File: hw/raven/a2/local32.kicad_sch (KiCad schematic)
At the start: 94 parts, among them J301 SIMM72, J302 SIMM72, J303 SIMM72, J304 SIMM72, J305 PWM, J306 Pinhdr_01x03, J307 USB2Header, J308 ARGB, U301 CH559L, U302 CH334R, U303 XR68M752, U304 CH213K, U305 MAX3245CAI+T, U306 W5100S-L, U307 74LVC1G19, X301 24Mhz (3.3V), Y301 12Mhz, Y302 25Mhz

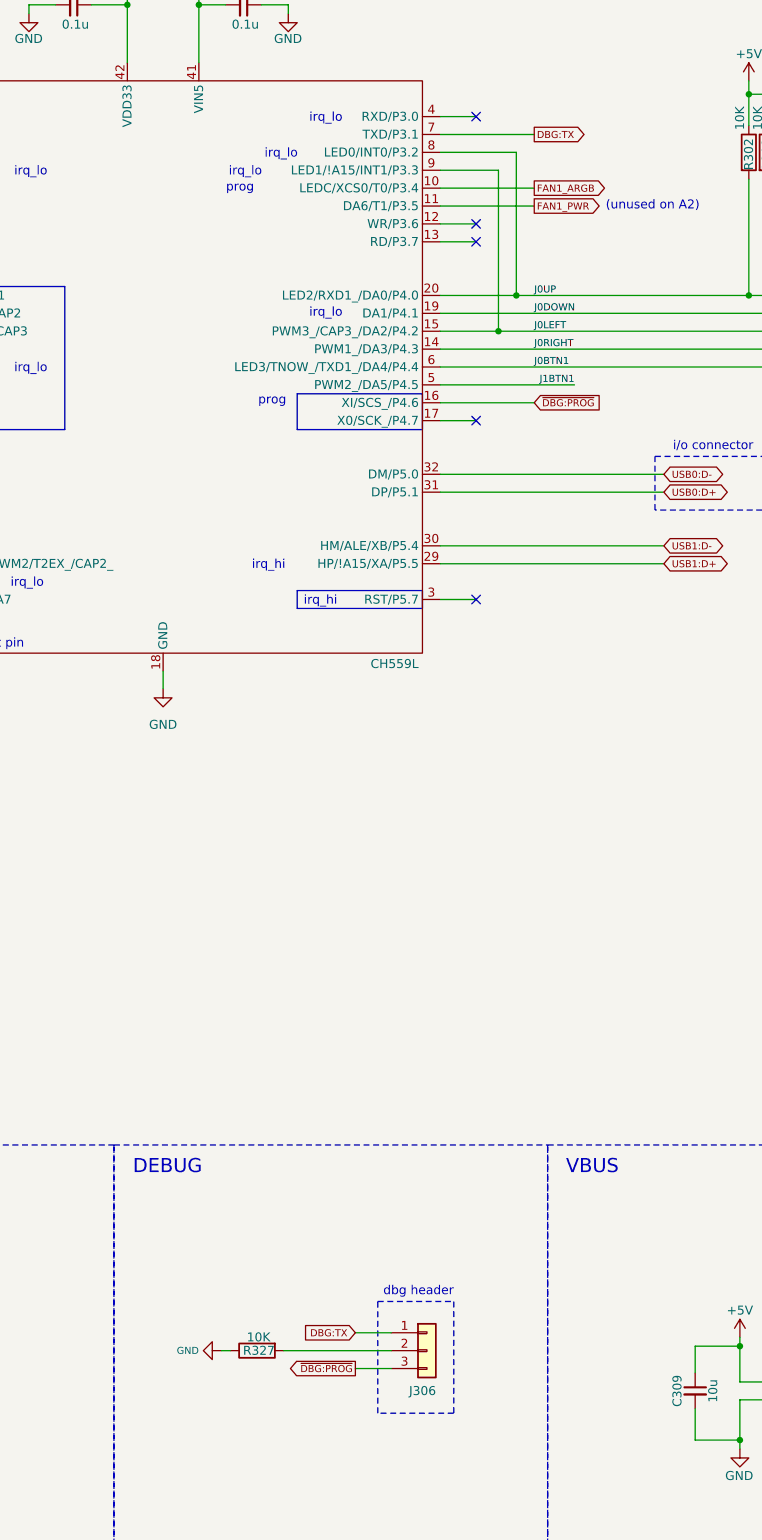
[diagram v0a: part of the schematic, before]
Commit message: minor fixes
- replace IDE header footprint and part
- fix floating (unused) inputs on U102
- removed ckbd debug pads
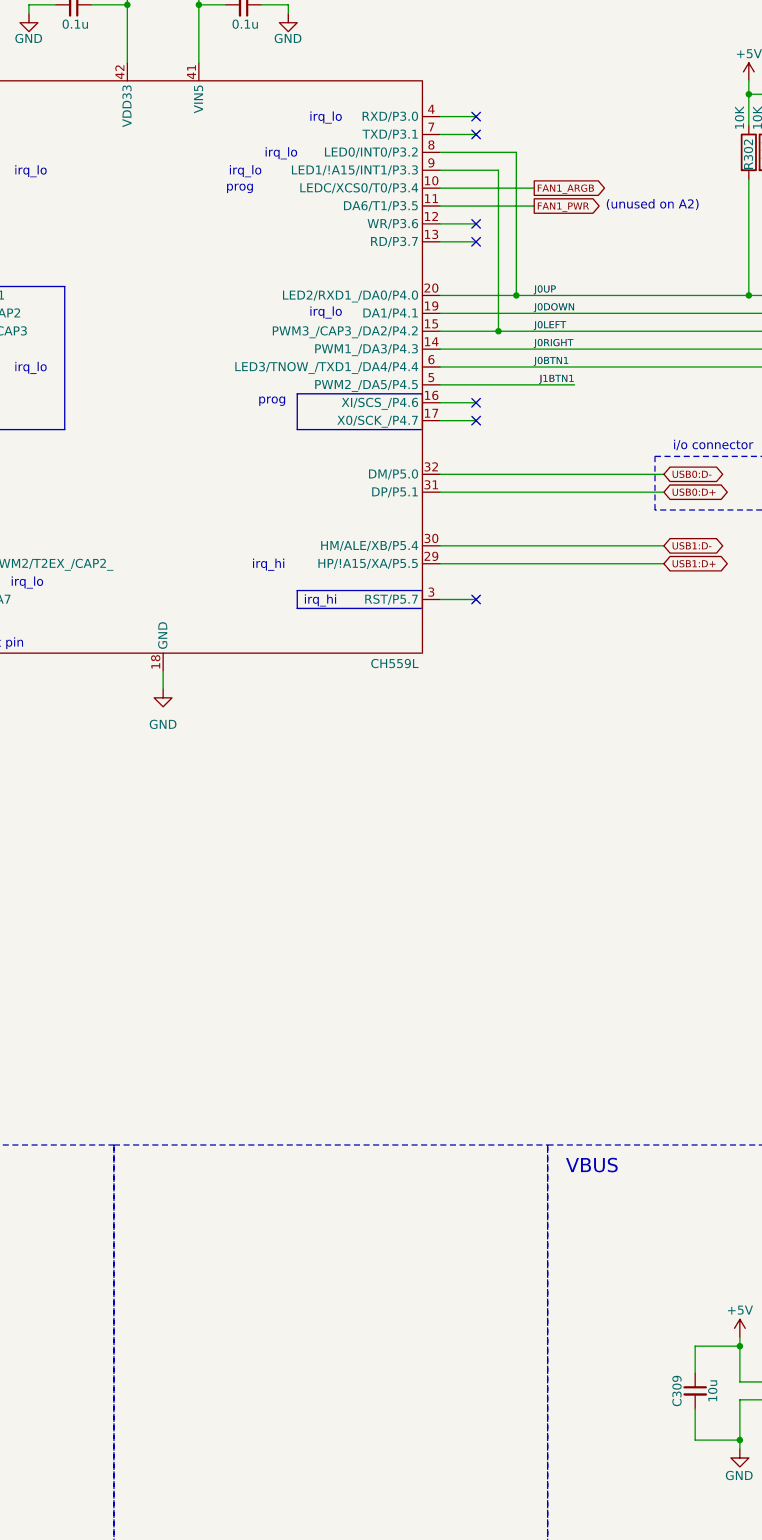
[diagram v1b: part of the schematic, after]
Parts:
- removed J306: Pinhdr_01x03, Connector_PinHeader_2.54mm:PinHeader_1x03_P2.54mm_Vertical, symbol Connector_Generic:Conn_01x03
- removed R327: 10K, Resistor_SMD:R_1206_3216Metric_Pad1.30x1.75mm_HandSolder, symbol Device:R
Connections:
- net DBG:TX: no longer names the net of U301.7 (TXD/P3.1)
- net ~{DBG:PROG}: no longer names the net of U301.16 (XI/SCS_/P4.6)
- no-connect marks 34 -> 36
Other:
- note removed: "DEBUG"
- note removed: "dbg header"

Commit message: A2 rework
- reworking top-left area for dsp56303
- internal speaker header for YM
- software controlled volume for YM
- misc routing cleanup
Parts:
- removed C303, C304, C328, C329: 33p, Capacitor_SMD:C_1206_3216Metric_Pad1.33x1.80mm_HandSolder, symbol 68k:c_100nf_smd1206
- removed C306, C307: 10u, Capacitor_SMD:C_1206_3216Metric_Pad1.33x1.80mm_HandSolder, symbol 68k:c_100nf_smd1206
- removed C316, C317, C318, C319, C320, C321, C322, C323, C324, C325, C326, C327: 0.1u, Capacitor_SMD:C_1206_3216Metric_Pad1.33x1.80mm_HandSolder, symbol 68k:c_100nf_smd1206
- removed J307: USB2Header, 68k:USB2Header, symbol 68k:USB2Header
- removed L301, L302, L303: 120, Inductor_SMD:L_1206_3216Metric_Pad1.42x1.75mm_HandSolder, symbol Device:L_Small
- removed R301, R317, R324: 1K, Resistor_SMD:R_1206_3216Metric_Pad1.30x1.75mm_HandSolder, symbol Device:R
- removed R332, R334: 49.9, Resistor_SMD:R_1206_3216Metric_Pad1.30x1.75mm_HandSolder, symbol Device:R
- removed R340, R341: 10K, Resistor_SMD:R_1206_3216Metric_Pad1.30x1.75mm_HandSolder, symbol Device:R
- removed R342: 1M, Resistor_SMD:R_1206_3216Metric_Pad1.30x1.75mm_HandSolder, symbol Device:R
- removed R343: 12.3K, Resistor_SMD:R_1206_3216Metric_Pad1.30x1.75mm_HandSolder, symbol Device:R
- removed U302: CH334R, Package_SO:QSOP-16_3.9x4.9mm_P0.635mm, symbol 68k:CH334R
- removed U306: W5100S-L, Package_QFP:LQFP-48_7x7mm_P0.5mm, symbol 68k:W5100S-L
- removed U307: 74LVC1G19, Package_TO_SOT_SMD:SOT-23-6_Handsoldering, symbol 74xGxx:74LVC1G19
- removed Y301: 12Mhz, 68k:ECS120203XENTR, symbol Device:Crystal
- removed Y302: 25Mhz, 68k:ECS120203XENTR, symbol Device:Crystal
- added J306: ESSI0, 68k:ESSI, symbol 68k:ESSI
- added J307: ESSI1, 68k:ESSI, symbol 68k:ESSI
- added R125, R126, R127, R128, R129, R130, R131: 1K, Resistor_SMD:R_1206_3216Metric_Pad1.30x1.75mm_HandSolder, symbol Device:R
- added R132, R133, R134, R135, R137, R138, R139, R140, R141, R143: 33, Resistor_SMD:R_1206_3216Metric_Pad1.30x1.75mm_HandSolder, symbol Device:R
- added R327: 10K, Resistor_SMD:R_1206_3216Metric_Pad1.30x1.75mm_HandSolder, symbol Device:R
- added U302: PCM5102A, Package_SO:TSSOP-20_4.4x6.5mm_P0.65mm, symbol Audio:PCM5102A
- added U306: SN74LVC1G14DBV, Package_TO_SOT_SMD:SOT-23-5_HandSoldering, symbol 74xGxx:SN74LVC1G14DBV
- added U307: 74LVC1G08, Package_TO_SOT_SMD:SOT-23-5_HandSoldering, symbol 74xGxx:74LVC1G08
- added U308: DSP56303, 68k:DSP56303, symbol 68k:DSP56303
- added U309, U310, U311: AS7C31024B-xxTJ, 68k:SOJ32_SRAM_300, symbol Memory_RAM:AS7C31024B-xxTJ
- R325, R329, R330, R331: value 1K -> 10K; Manufacturer_Part_Number RT1206FRE071KL -> RT1206FRE0710KL
- R333, R335: value 49.9 -> 10K; Manufacturer_Part_Number RT1206DRD0749R9L -> RT1206FRE0710KL
- R336, R337, R338, R339: value 3.3 -> 10K; Manufacturer_Part_Number RT1206FRE073R3L -> RT1206FRE0710KL
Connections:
- net ETH_1V2A is gone; now on net +3.3V: C315.1
- net RJ:TRD1- is gone; now on net +3.3V: R337.1
- net RJ:TRD2- is gone; now on net +3.3V: R339.1
- net ~{IRQ_ETH} is gone; now on net GND: U303.40 (~{CDA})
- net +3.3V: now also R333.1, R335.2, R336.2, R338.1, J306.2 (Pin_2), J307.2 (Pin_2), R125.1, R126.1, R127.1, R128.1, R129.1, R130.1, R131.1, R327.1, U306.5 (VCC)
- net +5V: now also J306.10 (Pin_10), J307.10 (Pin_10)
- net A2: now also U308.33 (HA0)
- net A3: now also U308.32 (HA1)
- net A4: now also U308.31 (HA2)
- net D24: now also U308.43 (H0)
- net D25: now also U308.42 (H1)
- net D26: now also U308.41 (H2)
- net D27: now also U308.40 (H3)
- net D28: now also U308.37 (H4)
- net D29: now also U308.36 (H5)
- net D30: now also U308.35 (H6)
- net D31: now also U308.34 (H7)
- net GND: now also U303.38 (~{CTSA}), U303.39 (~{DSRA}), U305.12 (T3IN), J306.1 (Pin_1), J307.1 (Pin_1), U302.10 (DEMP), U302.12 (SCK), U302.16 (FMT), U306.3 (GND), U307.3 (GND), U308.104 (GNDD), U308.112 (GNDD), U308.120 (GNDD), U308.127 (GNDQ), U308.130 (GNDD), U308.141 (TCK), U308.19 (GNDQ), U308.26 (GNDS), U308.39 (GNDH), U308.47 (GNDP), U308.48 (GNDP), U308.54 (GNDQ), U308.58 (GNDC), U308.62 (*TA), U308.66 (GNDC), U308.71 (*BG), U308.75 (GNDA), U308.81 (GNDA), U308.87 (GNDA), U308.9 (GNDS), U308.90 (GNDQ), U308.96 (GNDA), U309.16 (GND), U310.16 (GND), U311.16 (GND)
- net IKBD_RX: now also R325.2
- net IKBD_TX: now also R331.2
- net R~{W}: now also U308.22 (HR*W)
- net at R335.1: now also U308.23 (*HACK)
- net ~{DSP_TRIG}: now reaches R339.2
- net ~{DSP_TRIG}: now also U303.20 (~{DSRB}), U308.13 (PE0/RXD)
- net at R337.2: now also U308.6 (*NMI/PINIT)
- net DSP_TX: now reaches R338.2
- net DSP_TX: now also J306.9 (Pin_9), U308.14 (PE1/TXD)
- net UART1_CONN: now reaches U305.21 (~{INVALID})
- net UART1_CONN: now also U303.16 (~{CDB})
- net IKBD_DBG_TX: now reaches U301.7 (TXD/P3.1)
- net IKBD_DBG_TX: now also R333.2, J307.9 (Pin_9)
- removed net IKBD_CTS: R325.2, U301.36 (P0.4/AD4/UCTS), U303.33 (~{RTSA})
- net IKBD_RTS: no longer names the net of U301.39 (P0.1/AD1/URTS)
- net IKBD_RTS: no longer U303.38 (~{CTSA})
- net RJ:TRD1+: no longer names the net of R336.1
- net RJ:TRD1+: now also U308.64 (*BB); no longer R335.2
- removed net RJ:TRD2+: R333.2, R338.1
- net UART1:CDB: no longer names the net of U305.19 (R1OUT)
- net UART1:CDB: no longer U303.16 (~{CDB})
- net UART1:DSRB: no longer names the net of U305.18 (R2OUT)
- net UART1:DSRB: no longer U303.20 (~{DSRB})
- removed net UART1:DTRB: R331.2, U303.35 (~{DTRB}), U305.12 (T3IN)
- net UART1:RIB: no longer names the net of U305.15 (R5OUT)
- net UART1:RIB: no longer U303.21 (~{RIB})
- new net: R129.2, U308.137 (*IRQA/MODA)
- new net: R127.2, U308.135 (*IRQC/MODC)
- new net: R128.2, U308.136 (*IRQB/MODB)
- new net: U306.4, U308.44 (*RESET)
- new net DSP_A0: U308.72 (A0), U309.31 (A15), U310.31 (A15), U311.31 (A15)
- new net DSP_A1: U308.73 (A1), U309.3 (A14), U310.3 (A14), U311.3 (A14)
- new net DSP_A10: U308.88 (A10), U309.25 (A11), U310.25 (A11), U311.25 (A11)
- new net DSP_A11: U308.89 (A11), U309.9 (A3), U310.9 (A3), U311.9 (A3)
- new net DSP_A12: U308.92 (A12), U309.10 (A2), U310.10 (A2), U311.10 (A2)
- new net DSP_A13: U308.93 (A13), U309.23 (A10), U310.23 (A10), U311.23 (A10)
- new net DSP_A14: U308.94 (A14), U309.11 (A1), U310.11 (A1), U311.11 (A1)
- new net DSP_A15: U308.97 (A15), U309.12 (A0), U310.12 (A0), U311.12 (A0)
- new net DSP_A16: U308.98 (A16)
- new net DSP_A17: U308.99 (A17)
- new net DSP_A2: U308.76 (A2), U309.4 (A12), U310.4 (A12), U311.4 (A12)
- new net DSP_A3: U308.77 (A3), U309.5 (A7), U310.5 (A7), U311.5 (A7)
- new net DSP_A4: U308.78 (A4), U309.28 (A13), U310.28 (A13), U311.28 (A13)
- new net DSP_A5: U308.79 (A5), U309.6 (A6), U310.6 (A6), U311.6 (A6)
- new net DSP_A6: U308.82 (A6), U309.27 (A8), U310.27 (A8), U311.27 (A8)
- new net DSP_A7: U308.83 (A7), U309.7 (A5), U310.7 (A5), U311.7 (A5)
- new net DSP_A8: U308.84 (A8), U309.26 (A9), U310.26 (A9), U311.26 (A9)
- new net DSP_A9: U308.85 (A9), U309.8 (A4), U310.8 (A4), U311.8 (A4)
- new net DSP_D0: U308.100 (D0), U309.21 (I/O7)
- new net DSP_D1: U308.101 (D1), U309.13 (I/O0)
- new net DSP_D10: U308.114 (D10), U310.13 (I/O0)
- new net DSP_D11: U308.115 (D11), U310.19 (I/O5)
- new net DSP_D12: U308.116 (D12), U310.14 (I/O1)
- new net DSP_D13: U308.117 (D13), U310.18 (I/O4)
- new net DSP_D14: U308.118 (D14), U310.15 (I/O2)
- new net DSP_D15: U308.121 (D15), U310.17 (I/O3)
- new net DSP_D16: U308.122 (D16), U311.21 (I/O7)
- new net DSP_D17: U308.123 (D17), U311.20 (I/O6)
- new net DSP_D18: U308.124 (D18), U311.13 (I/O0)
- new net DSP_D19: U308.125 (D19), U311.19 (I/O5)
- new net DSP_D2: U308.102 (D2), U309.20 (I/O6)
- new net DSP_D20: U308.128 (D20), U311.14 (I/O1)
- new net DSP_D21: U308.131 (D21), U311.18 (I/O4)
- new net DSP_D22: U308.132 (D22), U311.15 (I/O2)
- new net DSP_D23: U308.133 (D23), U311.17 (I/O3)
- new net DSP_D3: U308.105 (D3), U309.14 (I/O1)
- new net DSP_D4: U308.106 (D4), U309.19 (I/O5)
- new net DSP_D5: U308.107 (D5), U309.15 (I/O2)
- new net DSP_D6: U308.108 (D6), U309.18 (I/O4)
- new net DSP_D7: U308.109 (D7), U309.17 (I/O3)
- new net DSP_D8: U308.110 (D8), U310.21 (I/O7)
- new net DSP_D9: U308.113 (D9), U310.20 (I/O6)
- new net DSP_RESET: R327.2, U303.33 (~{RTSA}), U306.2
- new net ESSI0_SC0: J306.3 (Pin_3), U308.12 (PC0/SC00)
- new net ESSI0_SC1: J306.5 (Pin_5), U308.4 (PC1/SC01)
- new net ESSI0_SC2: J306.7 (Pin_7), U308.3 (PC2/SC02)
- new net ESSI0_SCK: J306.8 (Pin_8), U308.17 (PC3/SCK0)
- new net ESSI0_SRD: J306.6 (Pin_6), U308.7 (PC4/SRD0)
- new net ESSI0_STD: J306.4 (Pin_4), U308.10 (PC5/STD0)
- new net ESSI1_SC0: J307.3 (Pin_3), U308.11 (PD0/SC10)
- new net ESSI1_SC1: J307.5 (Pin_5), U308.144 (PD1/SC11)
- new net ESSI1_SC2: J307.7 (Pin_7), U308.143 (PD2/SC12)
- new net ESSI1_SCK: J307.8 (Pin_8), U308.16 (PD3/SCK1)
- new net ESSI1_SRD: J307.6 (Pin_6), U308.1 (PD4/SRD1)
- new net ESSI1_STD: J307.4 (Pin_4), U308.2 (PD5/STD1)
- new net ~{DSP_AA0}: R130.2, U307.1, U308.70 (*RAS0/AA0)
- new net ~{DSP_AA1}: R131.2, U307.2, U308.69 (*RAS1/AA1), U309.2 (A16), U310.2 (A16), U311.2 (A16)
- new net ~{DSP_CS}: U308.21 (*HDS), U308.30 (*HCS)
- new net ~{DSP_HREQ}: R125.2, U303.21 (~{RIB}), U308.24 (*HREQ)
- new net ~{DSP_IRQ}: R126.2, U303.35 (~{DTRB}), U308.134 (*IRQD/MODD)
- new net ~{DSP_RAM_CS}: U307.4, U309.22 (~{CS1}/~{CE1}), U310.22 (~{CS1}/~{CE1}), U311.22 (~{CS1}/~{CE1})
- new net ~{DSP_RD}: U308.68 (*RD), U309.24 (~{OE}), U310.24 (~{OE}), U311.24 (~{OE})
- new net ~{DSP_WR}: U308.67 (*WR), U309.29 (~{WE}), U310.29 (~{WE}), U311.29 (~{WE})
- no-connect marks 36 -> 55
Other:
- note added: "100uF cap Panasonic EB1A101S"
- note added: "10uF cap to gnd"
- note added: "3.3v = low latency"
- note added: "3V only"
- note added: "5V tolerant"
- note added: "DSP_IRQ <- DSP_IRQ -> DSP_RESET -> pullups on irq. DSP Reset Circuit: UART DTRB 10kΩ Pull-up to VCC. UART DTRB 74LVC1G14 (Schmitt NOT Gate) Input. NOT Gate Output DSP /RESET. Result: Permanent Reset at power-on. Drive DTRB Low in BIOS to start DSP."
- note added: "Differences from standalone CKBD upgrade: - PWR_SW moved from P0.3 to P0.0 - FAN1_PWM added on P2.5 - FAN1_RGB added on P3.4 - FAN1_PWR removed from P3.5 - PS2M removed from P3.2, P3.3 - PS2K removed from P3.6, P3.7 - J0UP added on P3.2 (for irq) - J0LEFT added on P3.3 (for irq)"
- note added: "HI08-MC68302 bootstrap mode."
- note added: "Not 5V tolerant - CLKOUT - PCAP - EXTAL - XTAL"
- note added: "PLL Capacitor-An input connecting an off-chip capacitor to the PLL filter. Connect one capacitor terminal to PCAP and the other terminal to VCCP. If the PLL is not used, PCAP can be tied to VCC, GND, or left floating."
- note added: "PLL Ground Ground dedicated for PLL use. The connection should be provided with an extremely low-impedance path to ground. VCCP should be bypassed to GNDP by a 0.47 µF capacitor located as close as possible to the chip package. PLL Ground 1 Ground dedicated for PLL use. The connection should be provided with an extremely low-impedance path to ground."
- note added: "RXD and SCLK can also be configured as GPIO signals."
- note added: "generic dsp->host irq trigger"
- note added: "or DSP_AA1 whichever is best for routing"
- note added: "oscillator, either: 22.5792 MHz 11.2896 MHz"
- note added: "pll x4/x5 = 90.3168MHz"
- note added: "pullup 3.3v to unmute"
- note added: "static mcr inputs pwr_sw jumpers (failsafe mode jumper?)"
- note added: "todo footprint"
- note removed: "0000 : SPI Mode 010X : BUS Mode"
- note removed: "12.3k 1% resistor"
- note removed: "25Mhz 1.2V"
- note removed: "Differences from standalone CKBD upgrade: - PWR_SW moved from P0.3 to P0.0 - IKBD_RTS added on P0.1 - IKBD_CTS added on P0.4 - FAN1_PWM added on P2.5 - FAN1_RGB added on P3.4 - FAN1_PWR removed from P3.5 - PS2M removed from P3.2, P3.3 - PS2K removed from P3.6, P3.7 - J0UP added on P3.2 (for irq) - J0LEFT added on P3.3 (for irq)"
- note removed: "Ethernet"
- note removed: "Optional Not included in CH334R datasheet"
- note removed: "Optional damping for EMI reduction."
- note removed: "Or general GPIO between UART and CKBD"
- note removed: "RSET_BG is the most important analog pin and users should keep the noisy source away from this pin"
- note removed: "RST has built in pullup resistor. Recommended to leave floating when not reset."
- note removed: "To avoid the 100M overshoot, please place the 49.9 resistors and 0.1uF capacitor near the MDI pin of W5100S"
- note removed: "USB Header"
- note removed: "USB hub"
- note removed: "activity led (low/flash: state, high: down)"
- note removed: "collision led (low: collision, high: no collision)"
- note removed: "duplex led (low: full, high: half)"
- note removed: "internal oscillator: remove Y301 remove C304 0 ohm resistor on C303"
- note removed: "speed led (low: 100, high: 10)"
- note removed: "status led (low: up, high: down)"
- moved on the sheet: R323

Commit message: A2: DSP ram routing
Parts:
- removed U302: PCM5102A, Package_SO:TSSOP-20_4.4x6.5mm_P0.65mm, symbol Audio:PCM5102A
- removed U307: 74LVC1G08, Package_TO_SOT_SMD:SOT-23-5_HandSoldering, symbol 74xGxx:74LVC1G08
- added C303, C304, C306, C316: 0.1u, Capacitor_SMD:C_1206_3216Metric_Pad1.33x1.80mm_HandSolder, symbol 68k:c_100nf_smd1206
- added R136: 1K, Resistor_SMD:R_1206_3216Metric_Pad1.30x1.75mm_HandSolder, symbol Device:R
- added U312: 74LVC2G32, Package_SO:VSSOP-8_2.3x2mm_P0.5mm, symbol 74xGxx:74LVC2G32
- U309, U310, U311: Manufacturer_Name (none) -> Alliance Memory; Manufacturer_Part_Number (none) -> AS7C31024B-12TJCN
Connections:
- net ~{DSP_RAM_CS} is gone; now on net GND: U309.22 (~{CS1}/~{CE1}), U310.22 (~{CS1}/~{CE1}), U311.22 (~{CS1}/~{CE1})
- net +3.3V: now also U309.32 (VCC), U310.32 (VCC), U311.32 (VCC), C303.2, C304.2, C306.2, C316.1, U312.8 (VCC); no longer R130.1, R131.1
- net DSP_A16: now also R130.1, U312.6
- net GND: now also R130.2, R131.2, C303.1, C304.1, C306.1, C316.2, R136.2, U312.4 (GND)
- net DSP_RAM_CS: now reaches U310.30 (CS2/CE2)
- net DSP_RAM_CS: now also U309.30 (CS2/CE2), U311.30 (CS2/CE2), U312.7
- net ~{DSP_AA0} renamed DSP_AA0
- net DSP_AA0: now also R131.1, U312.2; no longer R130.2
- net ~{DSP_AA1} renamed DSP_SRAM_A16
- net DSP_SRAM_A16: now also U312.3; no longer R131.2, U308.69 (*RAS1/AA1)
- new net DSP_AA1: R136.1, U308.69 (*RAS1/AA1), U312.1, U312.5
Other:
- note added: "DSP"
- note added: "DSP RAM"
- note removed: "10uF cap to gnd"
- note removed: "3.3v = low latency"
- note removed: "or DSP_AA1 whichever is best for routing"
- note removed: "pullup 3.3v to unmute"
- note removed: "todo footprint"
- moved on the sheet: C309, C315, J305, J306, J307, J308, R125, R126, R127, R128, R129, R130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

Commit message: a2, reannotate
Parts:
- renumbered C305 to C303, C309 to C304, C308 to C305, C310 to C306, C311 to C307, C312 to C308, C313 to C309, C314 to C310, C303 to C311, C304 to C312, C306 to C313, C315 to C314, C316 to C315, J308 to J306, J306 to J307, J307 to J308, R333 to R301, R325 to R317, R331 to R318, R318 to R319, R319 to R320, R320 to R321, R321 to R322, R322 to R323, R323 to R324, R327 to R325, R328 to R327, R329 to R328, R330 to R329, R132 to R330, R133 to R331, R134 to R332, R135 to R333, R137 to R334, R138 to R335, R125 to R336, R139 to R337, R140 to R338, R141 to R339, R335 to R340, R143 to R341, R338 to R342, R339 to R343, R126 to R344, R127 to R345, R128 to R346, R129 to R347, R336 to R348, R337 to R349, R130 to R350, R131 to R351, R136 to R352, U303 to U302, U304 to U303, U305 to U304, U308 to U305, U309 to U306, U310 to U307, U311 to U308, U306 to U309, U312 to U310

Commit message: more a2 wip
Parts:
- removed R330, R331, R332, R333, R334, R337, R338, R339, R341: 33, Resistor_SMD:R_1206_3216Metric_Pad1.30x1.75mm_HandSolder, symbol Device:R
- removed X301: 24Mhz (3.3V), Oscillator:Oscillator_SMD_EuroQuartz_XO91-4Pin_7.0x5.0mm_HandSoldering, symbol Oscillator:XO91
- added C304, C305: 10u, Capacitor_SMD:C_1206_3216Metric_Pad1.33x1.80mm_HandSolder, symbol 68k:c_100nf_smd1206
- added C313: 0.47u, Capacitor_SMD:C_1206_3216Metric_Pad1.33x1.80mm_HandSolder, symbol 68k:c_100nf_smd1206
- added C318: 2.7n, Capacitor_SMD:C_1206_3216Metric_Pad1.33x1.80mm_HandSolder, symbol 68k:c_100nf_smd1206
- added C319: 4.7n, Capacitor_SMD:C_1206_3216Metric_Pad1.33x1.80mm_HandSolder, symbol 68k:c_100nf_smd1206
- added C321: 0.1u, Capacitor_SMD:C_1206_3216Metric_Pad1.33x1.80mm_HandSolder, symbol 68k:c_100nf_smd1206
- added J306: VUSB, Jumper:SolderJumper-2_P1.3mm_Open_RoundedPad1.0x1.5mm, symbol Jumper:SolderJumper_2_Open
- added J307: USB2Header, 68k:USB2Header, symbol 68k:USB2Header
- added J311: DSP_JTAG, 68k:SAMTEC_FTSH-105-01-L-D-K, symbol 68k:JTAG small - FTSH-105-01-L-D-K
- added R301, R345: 10K, Resistor_SMD:R_1206_3216Metric_Pad1.30x1.75mm_HandSolder, symbol Device:R
- added Y301: ASE-24.000MHZ-L-C-T, ASE24576MHZLCT, symbol 68k:ASE-24.000MHZ-L-C-T
- added Y302: ASELJ-E-22.5792MHz, ASELJE225792MHzLRT, symbol 68k:ASELJ-E-22.5792MHz-L-R-T
- J309: renamed from J307; footprint 68k:ESSI -> 68k:ESSI-BoxHeader
- J310: renamed from J308; footprint 68k:ESSI -> 68k:ESSI-BoxHeader
- R335: value 33 -> 220; Manufacturer_Part_Number RT1206FRE0733RL -> RT1206FRE07220RL
- renumbered C304 to C306, C305 to C307, C306 to C308, C307 to C309, C309 to C310, C310 to C311, C308 to C312, C311 to C314, C312 to C315, C313 to C316, C314 to C317, C315 to C320, J306 to J308, R301 to R302, R302 to R303, R303 to R304, R304 to R305, R305 to R306, R306 to R307, R307 to R308, R308 to R309, R309 to R310, R310 to R311, R311 to R312, R312 to R313, R313 to R314, R314 to R315, R315 to R316, R316 to R317, R317 to R318, R318 to R319, R319 to R320, R320 to R321, R321 to R322, R322 to R323, R323 to R324, R324 to R325, R325 to R326, R326 to R327, R327 to R328, R328 to R329, R329 to R330, R336 to R331, R340 to R332, R342 to R333, R343 to R334, R344 to R336, R345 to R337, R346 to R338, R347 to R339, R348 to R340, R349 to R341, R350 to R342, R351 to R343, R352 to R344
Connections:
- net +3.3V: now also U302.39 (~{DSRA}), U305.45 (VCCP), C313.2, C318.1, C319.1, C321.1, J311.01 (VTref), R301.1, Y301.1 (TRI-STATE_(STBY)), Y301.4 (VDD), Y302.1 (OE), Y302.4 (VDD)
- net +5V: now also J306.1 (A); no longer J309.10 (Pin_10), J310.10 (Pin_10)
- net DSP_TX: now also J309.10 (Pin_10), U301.4 (RXD/P3.0), R301.2; no longer J309.9 (Pin_9)
- net GND: now also C304.2, C305.2, C313.1, C321.2, J307.7 (GND), J307.8 (GND), J311.03 (GND), J311.05 (GND), J311.09 (GNDDetect), R345.1, Y301.2 (GND/CASE), Y302.2 (GND); no longer U302.38 (~{CTSA}), U302.39 (~{DSRA}), U305.141 (TCK)
- net IKBD_DBG_TX: now also J310.10 (Pin_10); no longer J310.9 (Pin_9)
- net UART1_CLK: now also Y301.3 (OUTPUT)
- net UART1_CONN: now also U302.38 (~{CTSA}); no longer U302.16 (~{CDB})
- net USB0:D+: now also J307.6 (DP1)
- net USB0:D-: now also J307.4 (DM1)
- net USB1:D+: now also J307.5 (DP0)
- net USB1:D-: now also J307.3 (DM0)
- net VUSB: now also C304.1, C305.1, J306.2 (B), J307.1 (+5V), J307.2 (+5V)
- net ~{DSP_HREQ}: now also U302.16 (~{CDB}); no longer U302.21 (~{RIB})
- net MODA: now reaches R339.2, U305.137 (*IRQA/MODA)
- net MODC: now reaches R337.2, U305.135 (*IRQC/MODC)
- net MODB: now reaches R338.2, U305.136 (*IRQB/MODB)
- net DSP_JTAG_TMO: now reaches U305.139 (TDO)
- net DSP_JTAG_TMO: now also J311.06 (TDO)
- net DSP_JTAG_TDI: now reaches U305.140 (TDI)
- net DSP_JTAG_TDI: now also J311.08 (TDI)
- net DSP_JTAG_TMS: now reaches U305.142 (TMS)
- net DSP_JTAG_TMS: now also J311.02 (TMS)
- net ~{DSP_TRIG2}: now reaches U305.15 (PE2/SCLK)
- net ~{DSP_TRIG2}: now also U302.21 (~{RIB}), R345.2
- net ~{DSP_RESET}: now reaches U305.44 (*RESET), U309.4
- net ~{DSP_RESET}: now also R335.1
- net PCAP: now reaches U305.46 (PCAP)
- net PCAP: now also C318.2, C319.2
- net ~{DSP_JTAG_DE}: now reaches U305.5 (*DE)
- net ~{DSP_JTAG_DE}: now also J311.07 (key)
- net at U305.55 (EXTAL): now also Y302.3 (OUTPUT)
- net at R335.2: now also J311.10 (nRESET)
- new net DSP_JTAG_CLK: J311.04 (TCK), U305.141 (TCK)
- no-connect marks 55 -> 51
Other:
- note added: "112mhz"
- note added: "22.5792 MHz MF = 4 = 90.3168 Mhz MF = 5 = 112.8960 Mhz core clock suitable for 44.1khz family"
- note added: "90mhz"
- note added: "A1=LO"
- note added: "A1=LO, A2=COM1 connection"
- note added: "A1=LO, A2=HI (rev indicator)"
- note added: "FREQ = MF * Ef * (2/PDF) Min Mhz = 30 Max Mhz = 200 PCAP (MF<=4) Min pF = (580 * MF) - 100 Max pF = (780 * MF) - 140 PCAP (MF>4) Min pF = (830 * MF) Max pF = (1470 * MF)"
- note added: "Freq 90mhz MF=4, PDF=2 PCAP min = 2220 PCAP max = 2980 PCAP use = 2.7nF Freq 112mhz MF=5, PDF=2 PCAP min = 4150 PCAP max = 7350 PCAP use = 4.7nF"
- note added: "RESET must be asserted when the chip is powered up. A stable EXTAL signal should be supplied before deassertion of RESET."
- note added: "USB header"
- note added: "custom"
- note added: "do not change, datasheet insist on 0.47u"
- note added: "int.pullup"
- note added: "low->high irq only"
- note removed: "5V tolerant"
- note removed: "RXD and SCLK can also be configured as GPIO signals."
- note removed: "generic dsp->host irq trigger"
- note removed: "oscillator, either: 22.5792 MHz 11.2896 MHz"
- note removed: "pll x4/x5 = 90.3168MHz"
- moved on the sheet: C312, C317, R302, R333, R334, R336, R337, R338, R339, U309

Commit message: A2: DAC for DSP and mix with YM
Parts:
- added C130, C131: 2.2u, Capacitor_SMD:C_1206_3216Metric_Pad1.33x1.80mm_HandSolder, symbol 68k:c_100nf_smd1206
- added C323, C324, C325, C326: 0.1u, Capacitor_SMD:C_1206_3216Metric_Pad1.33x1.80mm_HandSolder, symbol 68k:c_100nf_smd1206
- added U311: PCM5102A, Package_SO:TSSOP-20_4.4x6.5mm_P0.65mm, symbol Audio:PCM5102A
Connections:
- net +3.3V: now also C323.1, C324.1, C325.1, U311.1 (CPVDD), U311.20 (DVDD), U311.8 (AVDD)
- net ESSI0_SC2: now also U311.15 (LRCK)
- net ESSI0_SCK: now also U311.13 (BCK)
- net ESSI0_STD: now also U311.14 (DIN)
- net GND: now also C131.1, C323.2, C324.2, C325.2, C326.2, U311.10 (DEMP), U311.11 (FLT), U311.12 (SCK), U311.16 (FMT), U311.19 (DGND), U311.3 (CPGND), U311.9 (AGND)
- new net: C130.1, U311.4 (CAPM)
- new net: C130.2, U311.2 (CAPP)
- new net: C326.1, U311.18 (LDOO)
- new net: C131.2, U311.5 (VNEG)
- new net AUDIO_DSP_L: U311.6 (OUTL)
- new net AUDIO_DSP_R: U311.7 (OUTR)
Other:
- note added: "0 = mute 1 = unmute"
- note added: "ESSI expansion headers"
- note added: "ESSI0 DAC"
- note added: "JTAG header"
- note added: "de-emphasis off"
- note added: "i2s format"
- note added: "internal pll"
- note added: "normal latency"
- moved on the sheet: J309, J310, J311, R335

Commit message: A2: simplified DSP RAM connection
AA0 -> SRAM_CE
AA1 -> SRAM_A16

OMR register must be set to priority encoding disabled.
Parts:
- removed C320: 0.1u, Capacitor_SMD:C_1206_3216Metric_Pad1.33x1.80mm_HandSolder, symbol 68k:c_100nf_smd1206
- removed R342, R343: 1K, Resistor_SMD:R_1206_3216Metric_Pad1.30x1.75mm_HandSolder, symbol Device:R
- removed U310: 74LVC2G32, Package_SO:VSSOP-8_2.3x2mm_P0.5mm, symbol 74xGxx:74LVC2G32
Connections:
- net DSP_RAM_CS is gone; now on net +3.3V: U306.30 (CS2/CE2), U307.30 (CS2/CE2), U308.30 (CS2/CE2)
- net DSP_SRAM_A16 is gone; now on net DSP_AA1: U306.2 (A16), U307.2 (A16), U308.2 (A16)
- net +3.3V: now also R344.1
- net DSP_AA1: no longer R344.1
- net GND: no longer R344.2, U306.22 (~{CS1}/~{CE1}), U307.22 (~{CS1}/~{CE1}), U308.22 (~{CS1}/~{CE1})
- net DSP_AA0 renamed ~{DSP_AA0}
- net ~{DSP_AA0}: now also R344.2, U306.22 (~{CS1}/~{CE1}), U307.22 (~{CS1}/~{CE1}), U308.22 (~{CS1}/~{CE1})
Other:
- note added: "A16"
- note added: "CE2"
- note added: "logical physical P 00000-0FFFF 00000-0FFFF Y 00000-0FFFF 00000-0FFFF X 00000-0FFFF 10000-1FFFF DSP_AA0 P,Y SRAM_CE1 active low DSP_AA1 X SRAM_A16 active high"
- note added: "~{CE1}"
- note added: "~{OE}"
- note added: "~{WE}"
- moved on the sheet: C314, C315, C316, U306, U307, U308
